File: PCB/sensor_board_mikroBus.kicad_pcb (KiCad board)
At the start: 2 copper layers, 25.4 x 28.6 mm, 22 parts, among them J1 Molex_0475710001, P1 HEADER_M_2.54MM_1R8P_ST_AU_PTH, P2 HEADER_M_2.54MM_1R8P_ST_AU_PTH, U1 MCP3201, U2 MCP3201, U3 MCP1501-SOT-23, U4 HIH-5030-001, U5 AD592BN

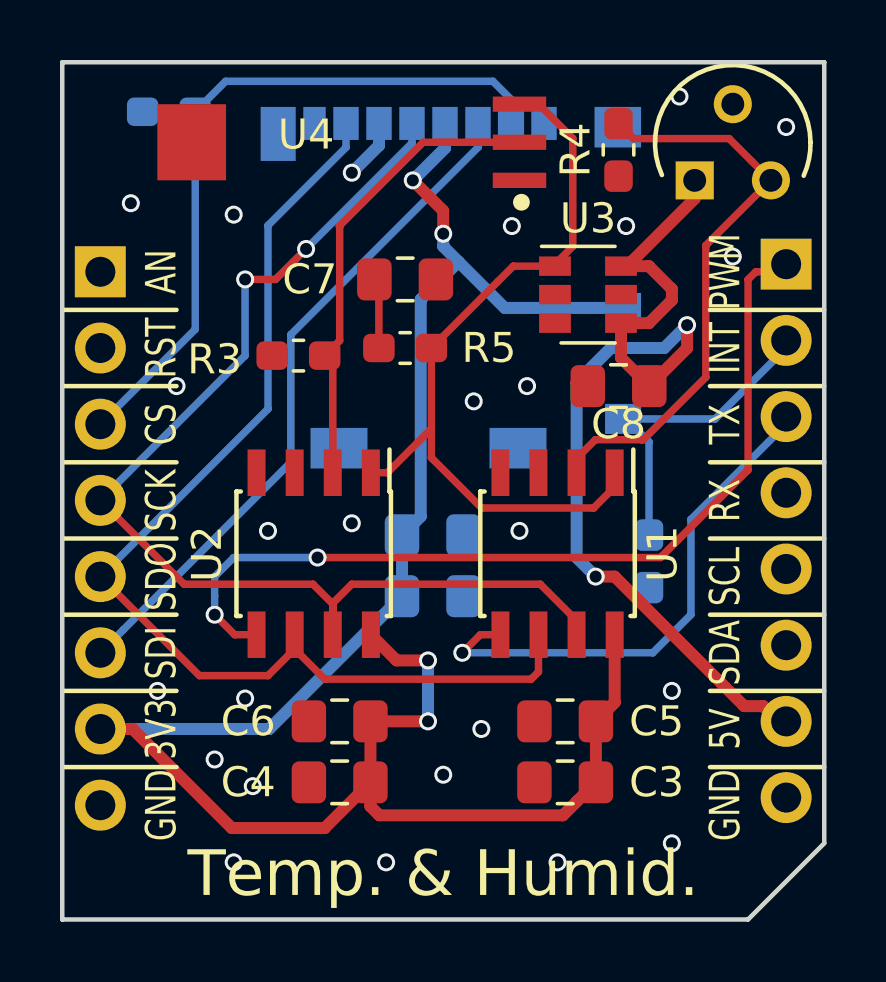
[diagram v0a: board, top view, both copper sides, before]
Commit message: PCB: Change sdcard pin connected to ground.
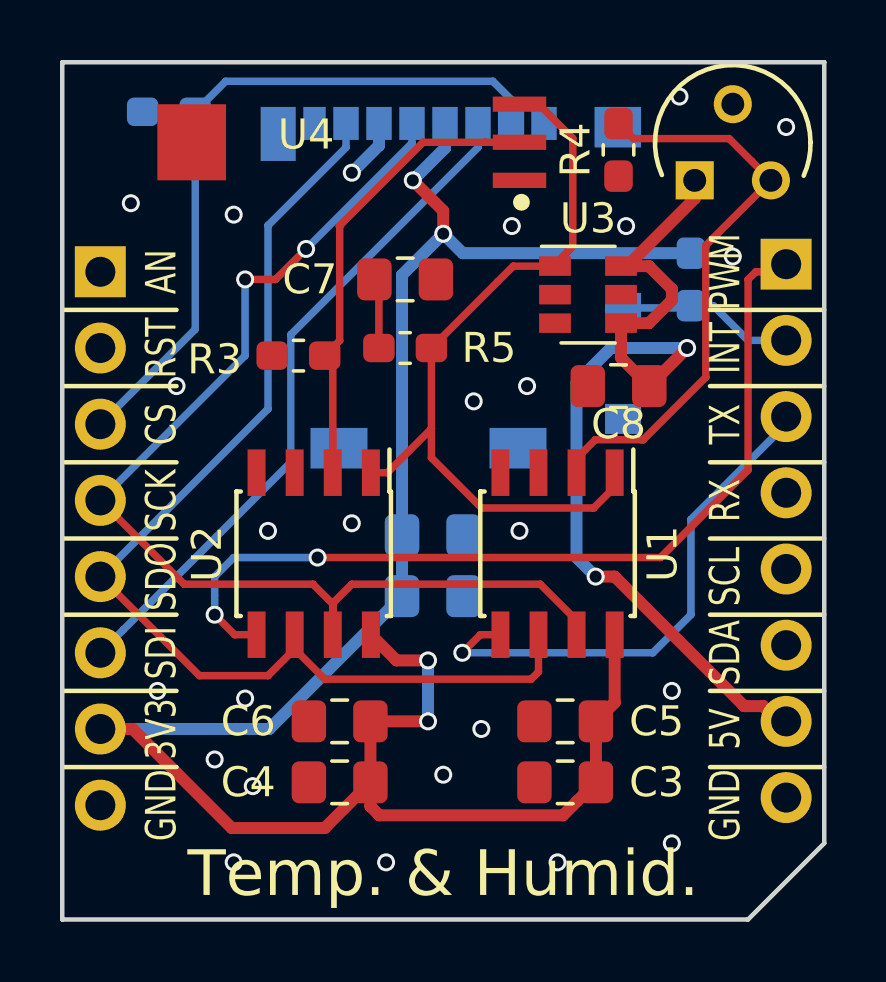
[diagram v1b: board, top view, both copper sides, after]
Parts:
- moved R2 9.50 mm to (132.0, 105.0), turned to 90 degrees
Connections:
- J1 pad 10: INT -> GND
- J1 pad 9: +3.3V -> INT
- R2 pad 2: GND -> +3.3V
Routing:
- net INT: track 10.7 -> 5.95 mm
- net +3.3V: track 68.9 -> 70.9 mm
- net +5V: track 33.2 -> 32.1 mm

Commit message: PCB: Update revision
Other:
- board text added: "HW REV. 1.1"
- board text removed: "HW REV. 1.0"
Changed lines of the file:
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@@
     (effects (font (size 1.016 0.762) (thickness 0.1524)) (justify mirror))
   )
-  (gr_text "HW REV. 1.0" (at 115.316 125.349) (layer B.SilkS)
+  (gr_text "HW REV. 1.1" (at 115.316 125.349) (layer B.SilkS)
     (effects (font (size 1.016 0.762) (thickness 0.1524)) (justify mirror))
   )

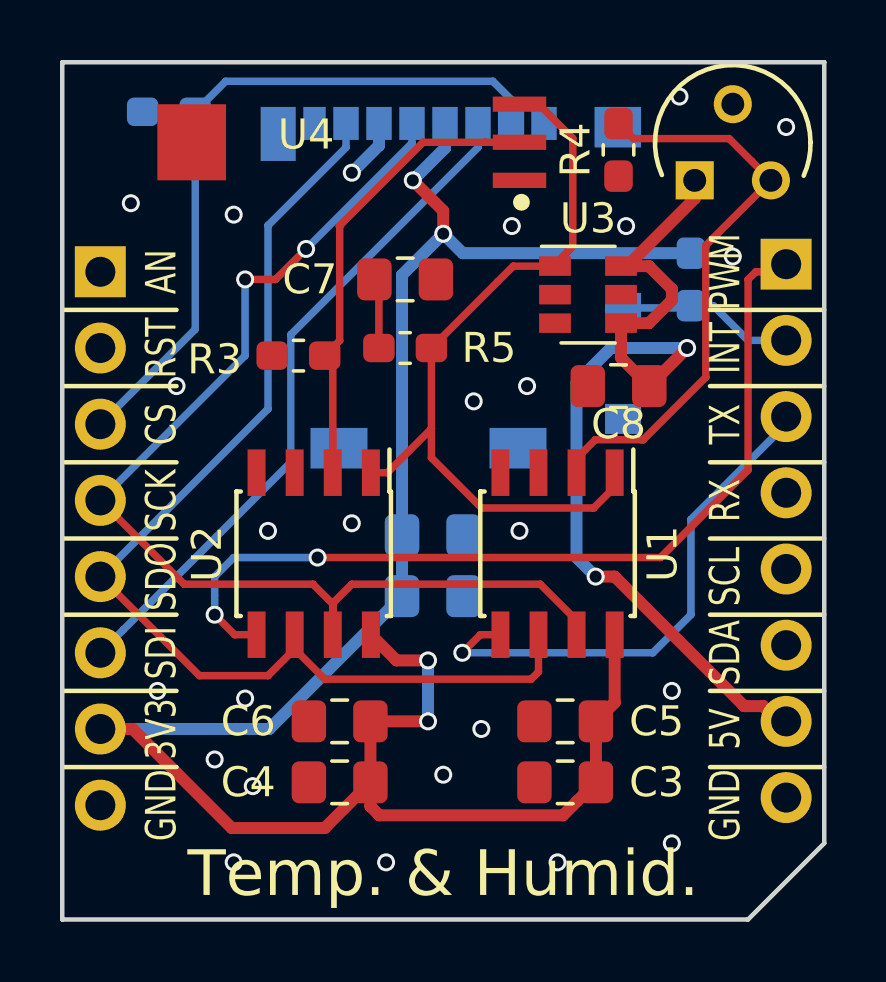
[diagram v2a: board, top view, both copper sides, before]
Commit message: PCB: Fix noise generated by sensor in Vref
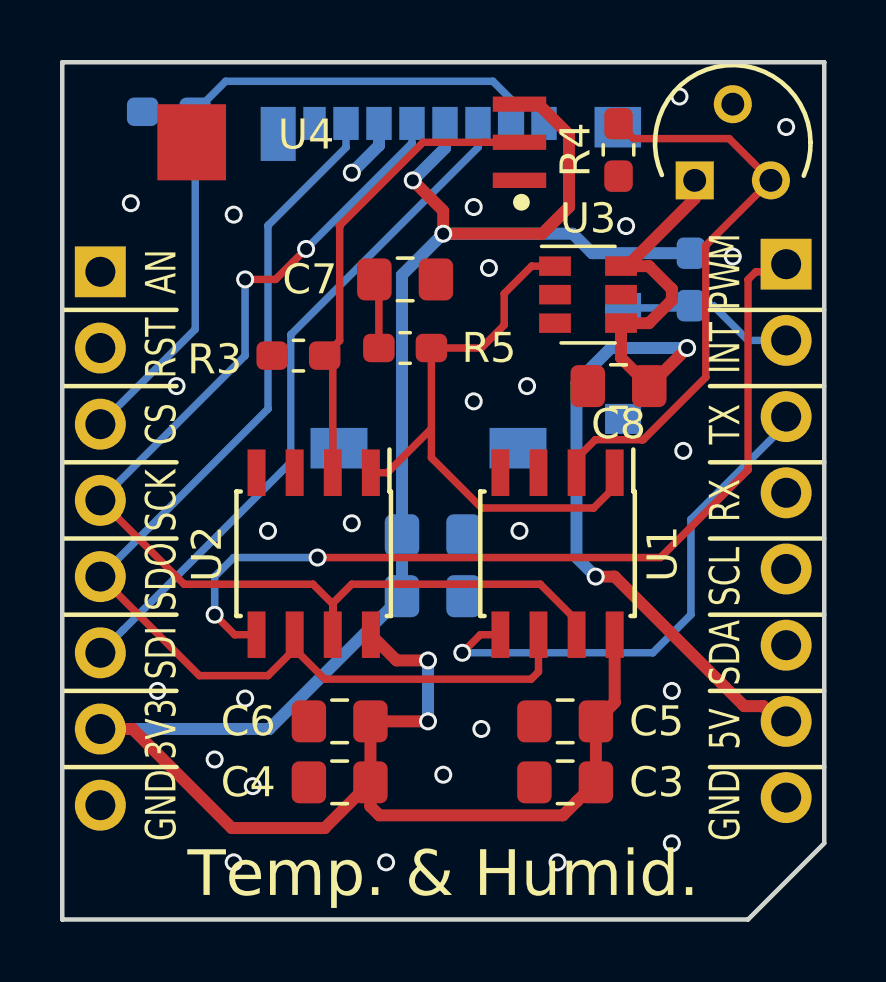
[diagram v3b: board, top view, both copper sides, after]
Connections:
- U4 pad 3: Vref -> +3.3V
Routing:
- net +3.3V: track 70.9 -> 80.0 mm
- net Vref: track 25.8 -> 19.7 mm
- net GND: vias 25 -> 27
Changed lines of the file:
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@@
     (thickness 1.6)
     (drawings 56)
-    (tracks 185)
+    (tracks 191)
     (zones 0)
     (modules 22)
@@
       (net 1 GND))
     (pad 3 smd rect (at 1.27 5.335 180) (size 1.78 0.51) (layers F.Cu F.Paste F.Mask)
-      (net 5 Vref))
+      (net 2 +3.3V))
   )
   (module Connector_PinHeader_2.54mm:PinHeader_1x08_P2.54mm_Vertical locked (layer B.Cu)
@@
   (via (at 129.794 103.251) (size 0.6) (drill 0.4) (layers F.Cu B.Cu) (net 1))
   (via (at 131.572 98.933) (size 0.6) (drill 0.4) (layers F.Cu B.Cu) (net 1))
-  (via (at 125.984 103.251) (size 0.6) (drill 0.4) (layers F.Cu B.Cu) (net 1))
+  (via (at 124.714 102.616) (size 0.6) (drill 0.4) (layers F.Cu B.Cu) (net 1))
   (via (at 117.094 118.999) (size 0.6) (drill 0.4) (layers F.Cu B.Cu) (net 1))
   (via (at 133.35 104.267) (size 0.6) (drill 0.4) (layers F.Cu B.Cu) (net 1))
@@
   (via (at 124.714 109.093) (size 0.6) (drill 0.4) (layers F.Cu B.Cu) (net 1))
   (via (at 117.856 113.411) (size 0.6) (drill 0.4) (layers F.Cu B.Cu) (net 1))
+  (via (at 131.699 110.744) (size 0.6) (drill 0.4) (layers F.Cu B.Cu) (net 1))
+  (via (at 125.222 104.648) (size 0.6) (drill 0.4) (layers F.Cu B.Cu) (net 1))
   (segment (start 117.896519 120.015) (end 122.323616 115.587903) (width 0.4) (layer B.Cu) (net 2) (status 20))
   (segment (start 112.268 120.015) (end 117.896519 120.015) (width 0.4) (layer B.Cu) (net 2) (status 10))
@@
   (via (at 123.698 103.505) (size 0.6) (drill 0.4) (layers F.Cu B.Cu) (net 2))
   (segment (start 122.323616 104.879384) (end 123.698 103.505) (width 0.4) (layer B.Cu) (net 2))
-  (segment (start 122.323616 113.555903) (end 122.323616 104.879384) (width 0.4) (layer B.Cu) (net 2))
-  (segment (start 124.347 104.154) (end 123.698 103.505) (width 0.4) (layer B.Cu) (net 2))
-  (segment (start 131.953 104.154) (end 124.347 104.154) (width 0.4) (layer B.Cu) (net 2))
+  (segment (start 122.323616 113.555903) (end 122.323616 104.879384) (width 0.4) (layer B.Cu) (net 2) (status 10))
+  (segment (start 123.698 103.505) (end 127 103.505) (width 0.4) (layer F.Cu) (net 2))
+  (segment (start 127 103.505) (end 127.889 102.616) (width 0.4) (layer F.Cu) (net 2))
+  (segment (start 126.874 99.187) (end 126.239 99.187) (width 0.4) (layer F.Cu) (net 2))
+  (segment (start 127.889 100.202) (end 126.874 99.187) (width 0.4) (layer F.Cu) (net 2))
+  (segment (start 127.889 102.616) (end 127.889 100.202) (width 0.4) (layer F.Cu) (net 2))
+  (segment (start 123.698 103.505) (end 128.016 103.505) (width 0.4) (layer B.Cu) (net 2))
+  (segment (start 128.665 104.154) (end 131.953 104.154) (width 0.4) (layer B.Cu) (net 2))
+  (segment (start 128.016 103.505) (end 128.665 104.154) (width 0.4) (layer B.Cu) (net 2))
   (segment (start 121.553 105.56) (end 121.403 105.41) (width 0.25) (layer F.Cu) (net 3) (status 30))
   (segment (start 121.553 107.315) (end 121.553 105.56) (width 0.25) (layer F.Cu) (net 3) (status 30))
@@
   (segment (start 131.064 107.315) (end 129.286 107.315) (width 0.4) (layer B.Cu) (net 4))
   (segment (start 131.064 107.315) (end 131.826 107.315) (width 0.4) (layer B.Cu) (net 4))
-  (segment (start 123.303 107.315) (end 125.523 105.095) (width 0.25) (layer F.Cu) (net 5) (status 10))
   (segment (start 121.835 111.473) (end 121.285 111.473) (width 0.25) (layer F.Cu) (net 5) (status 20))
   (segment (start 123.303 110.005) (end 121.835 111.473) (width 0.25) (layer F.Cu) (net 5))
   (segment (start 123.303 107.315) (end 123.303 110.005) (width 0.25) (layer F.Cu) (net 5) (status 10))
-  (segment (start 127.424 104.52) (end 128.016 103.928) (width 0.25) (layer F.Cu) (net 5) (status 10))
-  (segment (start 126.874 99.187) (end 126.239 99.187) (width 0.25) (layer F.Cu) (net 5) (status 30))
-  (segment (start 128.016 100.329) (end 126.874 99.187) (width 0.25) (layer F.Cu) (net 5) (status 20))
-  (segment (start 128.016 103.928) (end 128.016 100.329) (width 0.25) (layer F.Cu) (net 5))
-  (segment (start 126.031 104.587) (end 125.523 105.095) (width 0.25) (layer F.Cu) (net 5))
-  (segment (start 127.424 104.587) (end 126.031 104.587) (width 0.25) (layer F.Cu) (net 5) (status 10))
   (segment (start 129.413 111.948) (end 129.413 111.473) (width 0.25) (layer F.Cu) (net 5) (status 30))
   (segment (start 128.712 112.649) (end 129.413 111.948) (width 0.25) (layer F.Cu) (net 5) (status 20))
@@
   (segment (start 123.303 110.005) (end 123.303 110.975) (width 0.25) (layer F.Cu) (net 5))
   (segment (start 123.303 110.975) (end 124.977 112.649) (width 0.25) (layer F.Cu) (net 5))
+  (segment (start 123.303 107.315) (end 124.968 107.315) (width 0.25) (layer F.Cu) (net 5))
+  (segment (start 124.968 107.315) (end 125.73 106.553) (width 0.25) (layer F.Cu) (net 5))
+  (segment (start 126.644 104.587) (end 127.424 104.587) (width 0.25) (layer F.Cu) (net 5))
+  (segment (start 125.73 105.501) (end 126.644 104.587) (width 0.25) (layer F.Cu) (net 5))
+  (segment (start 125.73 106.553) (end 125.73 105.501) (width 0.25) (layer F.Cu) (net 5))
   (segment (start 119.751001 118.354001) (end 118.745 117.348) (width 0.25) (layer F.Cu) (net 6) (status 20))
   (segment (start 118.745 117.348) (end 118.745 116.873) (width 0.25) (layer F.Cu) (net 6) (status 30))
@@
   (segment (start 115.429 106.694) (end 112.268 109.855) (width 0.25) (layer B.Cu) (net 9) (status 20))
   (segment (start 115.429 99.441) (end 115.429 106.694) (width 0.25) (layer B.Cu) (net 9) (status 10))
-  (segment (start 131.878 105.979) (end 131.953 105.904) (width 0.25) (layer B.Cu) (net 10))
-  (segment (start 129.692 105.979) (end 131.878 105.979) (width 0.25) (layer B.Cu) (net 10))
-  (segment (start 131.953 105.904) (end 132.701 105.904) (width 0.25) (layer B.Cu) (net 10))
+  (segment (start 131.878 105.979) (end 131.953 105.904) (width 0.25) (layer B.Cu) (net 10) (status 30))
+  (segment (start 129.692 105.979) (end 131.878 105.979) (width 0.25) (layer B.Cu) (net 10) (status 30))
+  (segment (start 131.953 105.904) (end 132.701 105.904) (width 0.25) (layer B.Cu) (net 10) (status 10))
   (segment (start 132.701 105.904) (end 133.858 107.061) (width 0.25) (layer B.Cu) (net 10))
-  (segment (start 133.858 107.061) (end 135.128 107.061) (width 0.25) (layer B.Cu) (net 10))
+  (segment (start 133.858 107.061) (end 135.128 107.061) (width 0.25) (layer B.Cu) (net 10) (status 20))
   (segment (start 117.475 116.873) (end 116.746 116.873) (width 0.25) (layer F.Cu) (net 11) (status 10))
   (via (at 116.078 116.205) (size 0.6) (drill 0.4) (layers F.Cu B.Cu) (net 11))
@@
     (connect_pads (clearance 0.3))
     (min_thickness 0.254)
-    (fill yes (arc_segments 16) (thermal_gap 0.508) (thermal_bridge_width 0.508))
+    (fill yes (arc_segments 16) (thermal_gap 0.3) (thermal_bridge_width 0.508))
     (polygon
       (pts

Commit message: PCB: Update revision
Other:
- board text added: "HW REV. 1.2"
- board text removed: "HW REV. 1.1"
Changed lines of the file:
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@@
     (effects (font (size 1.016 0.762) (thickness 0.1524)) (justify mirror))
   )
-  (gr_text "HW REV. 1.1" (at 115.316 125.349) (layer B.SilkS)
+  (gr_text "HW REV. 1.2" (at 115.316 125.349) (layer B.SilkS)
     (effects (font (size 1.016 0.762) (thickness 0.1524)) (justify mirror))
   )
